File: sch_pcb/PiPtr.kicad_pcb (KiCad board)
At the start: 4 copper layers, 101.6 x 141.7 mm, 346 parts, among them J101 GLOBAL_LINK_LEFT, J102 GLOBAL_LINK_RIGHT, J107 RASPBERRY_PI, J111 FP_PIXEL, J112 AM2302, J113 I2C1_5V, J114 I2C0_3v3, J117 OLED_SSD1306, J204 DE9F, J301 SPARE, J302 SPARE, J303 SPARE, J304 SPARE, J305 AUX_IO_1, J306 SPARE, J307 SPARE, J308 AUX_IO_2, J309 SPARE, J310 SPARE, J313 SPARE, J314 SPARE, J404 DE9F, P301 Chassis, Q101 BSS138, Q102 BSS138, Q103 BSS138, Q104 BSS138, Q105 BSS138, Q201 2N7000, Q202 2N7000, Q203 2N7000, Q301 SPARE, Q302 SPARE, Q401 2N7000, Q402 2N7000, Q403 2N7000, U101 MCP23017, U102 IP4234CZ6, U103 MCP4351, U104 74HCT138, U105 74LV1T125, U107 MCP4351, U108 IP4234CZ6, U109 IP4234CZ6, U110 74LV1T125, U111 74LV1T125, U112 74LV1T125, U113 74LV1T125, U201 MCP6004N, U202 74LVC1G3157, U203 74LVC1G3157, U204 74LVC4066, U205 MCP6004N, U206 74LVC1G3157, U207 MCP6S26, U301 MCP23017, U302 SPARE, U303 SPARE, U304 MCP3008, U305 MCP1703A-2502/MB, U306 TPS54302, U307 IP4234CZ6, U401 MCP6004N, U402 74LVC1G3157, U403 74LVC1G3157, U404 74LVC4066, U405 MCP6004N, U406 74LVC1G3157, U407 MCP6S26, U501 CM108B, U502 CM108B, U503 TUSB2036, Y501 6MHz

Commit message: Add files via upload
Remove OLED connector
Remove extra bypass cap from third EEPOT
More routing - got the soundcards and usb hub done.  Only remaining big section is the DC-DC.  Still a bit of pain-in-the-tuchas traces that need to sneak across the board...
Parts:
- removed C110: 0.1u, lib:smd0603
- removed J114: I2C0_3v3, lib:SIL-6
- removed J117: OLED_SSD1306, lib:SIL-4
- removed TP105: TESTPOINT, lib:Wire_28AWG
- removed U109: IP4234CZ6, lib:SOT23-6
- added J103: RTC, lib:SIL-5, F.Cu at (104.1, 166.4)
- added R209: 10k, lib:smd0603, F.Cu at (78.0, 72.1)
- added R409: 10k, lib:smd0603, F.Cu at (142.8, 71.5)
- added R517: 15k, lib:smd0603, F.Cu at (95.0, 125.1)
- Q201, Q202, Q203, Q401, Q402, Q403: value 2N7000 -> BSS138
- moved C109 164.2 mm to (143.7, 63.1), turned to 270 degrees
- moved C307 151.0 mm to (108.7, 66.9), turned to 270 degrees
- moved C108 150.7 mm to (78.7, 63.6), turned to 270 degrees
- moved C306 148.8 mm to (105.9, 66.9), turned to 270 degrees
- moved C310 138.2 mm to (146.8, 107.9)
- moved C311 138.2 mm to (148.5, 107.9)
- moved C312 138.2 mm to (145.4, 107.8)
- moved C313 138.2 mm to (143.6, 107.8)
- moved R324 138.2 mm to (142.0, 107.8)
- moved U305 138.2 mm to (145.4, 103.3)
- moved J303 123.0 mm to (63.1, 129.9), turned to 90 degrees
- moved R306 120.4 mm to (60.1, 127.9), turned to 270 degrees
- moved R303 119.4 mm to (60.1, 130.9), turned to 270 degrees
- moved J302 118.0 mm to (63.1, 121.9), turned to 90 degrees
- moved C324 117.9 mm to (165.9, 136.6)
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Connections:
- U503 pad 6: +3V3 -> Net-(R517-Pad1)
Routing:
- net +3V3: track 15.1 -> 603.1 mm, vias 0 -> 8
- net /LINK2C: track 0.00 -> 127.0 mm, vias 0 -> 1
- net +5V: track 213.8 -> 339.5 mm, vias 9 -> 33
- net /SDA1_5: track 18.2 -> 141.7 mm, vias 2 -> 5
- net /LINK1C: track 0.00 -> 120.1 mm, vias 0 -> 1
- net /SCL1_5: track 21.0 -> 136.8 mm, vias 0 -> 4
- net GND: track 122.6 -> 235.6 mm, vias 65 -> 110
- net /~R47CS: track 0.00 -> 100.4 mm, vias 0 -> 4
- net SCLK_5: track 61.1 -> 160.0 mm, vias 2 -> 7
- net /~PGA2_CS: track 0.00 -> 89.9 mm, vias 0 -> 2
- net /CH2/TONE_FROM_PI: track 28.2 -> 102.8 mm, vias 2 -> 4
- net /~R03CS: track 0.00 -> 71.3 mm, vias 0 -> 4
- net /RX2_BUS1_EN: track 0.00 -> 69.1 mm, vias 0 -> 3
- net /RX2_BUS2_EN: track 0.00 -> 66.0 mm, vias 0 -> 3
- net /DHT_33: track 0.00 -> 64.4 mm, vias 0 -> 2
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- added copper zone on In2.Cu, net +5V
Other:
- board text added: "Pixel"
- board text added: "RTC"
- board text added: "Temp/Hum"

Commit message: Add files via upload
Fix sheet ordering in schematic
Finish routing (except USB connector...)
Still to do: USB connector, cleanup PCB, fix refdes positions
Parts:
- added LOGO301: MOUNTING_HOLE, lib:BOBCAT_LOGO, F.Cu at (154.8, 161.3)
- moved J307 71.7 mm to (108.3, 158.3)
- moved J306 56.4 mm to (92.5, 158.3)
- moved C308 48.2 mm to (131.8, 115.4), turned to 180 degrees
- moved C309 48.1 mm to (131.8, 113.9), turned to 180 degrees
- moved C322 22.5 mm to (143.3, 141.2), turned to 90 degrees
- moved C324 20.9 mm to (145.6, 141.2), turned to 90 degrees
- moved C323 17.9 mm to (147.8, 141.2), turned to 90 degrees
- moved C319 16.7 mm to (137.2, 140.9), turned to 180 degrees
- moved C325 16.0 mm to (149.8, 141.2), turned to 90 degrees
- moved C320 15.4 mm to (136.9, 143.1), turned to 180 degrees
- moved R327 11.8 mm to (135.9, 151.2), turned to 270 degrees
- moved R328 10.8 mm to (137.4, 151.2), turned to 90 degrees
- moved U306 6.54 mm to (136.9, 147.2), turned to 180 degrees
- moved R325 5.55 mm to (134.2, 148.2), turned to 90 degrees
- moved U105 5.28 mm to (94.8, 161.7)
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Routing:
- net /Spares, GPIO, and ADC/ADC_LIGHT: track 21.8 -> 248.7 mm, vias 0 -> 2
- net +2V5: track 52.9 -> 195.1 mm, vias 35 -> 37
- net /CH1/FROM_SOUNDCARD: track 0.00 -> 110.4 mm, vias 0 -> 6
- net +5V: track 339.5 -> 443.0 mm, vias 33 -> 43
- net /CH2/TO_SOUNDCARD: track 0.00 -> 95.6 mm, vias 0 -> 6
- net /CH2/FROM_SOUNDCARD: track 0.00 -> 94.5 mm, vias 0 -> 4
- net /SDA0_33: track 62.1 -> 143.3 mm, vias 0 -> 1
- net +12V: track 229.3 -> 306.6 mm, vias 1 -> 2
- net /CH1/TO_SOUNDCARD: track 0.00 -> 76.0 mm, vias 0 -> 2
- net /SCL0_33: track 59.7 -> 133.8 mm, vias 0 -> 1
- net MOSI_5: track 118.1 -> 185.3 mm, vias 4 -> 9
- net GND: track 235.6 -> 297.7 mm, vias 110 -> 123
- net MISO_5: track 76.6 -> 133.9 mm, vias 4 -> 7
- net /RX2_LOCAL_EN: track 17.9 -> 67.1 mm, vias 1 -> 4
- net +3V3: track 603.1 -> 631.6 mm, vias 8 -> 10
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- added copper zone on F.Cu, net +12V
- added copper zone on F.Cu, net +5V
- added copper zone on F.Cu, net GND
- added copper zone on B.Cu, net Net-(C321-Pad2)
- added copper zone on F.Cu, net Net-(C321-Pad2)
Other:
- net class Default: clearance 0.2 -> 0
- rule trace_clearance: 0.2 -> 0
- board text added: "MMRA PiPTR"
- board text removed: "LDR on front panel"

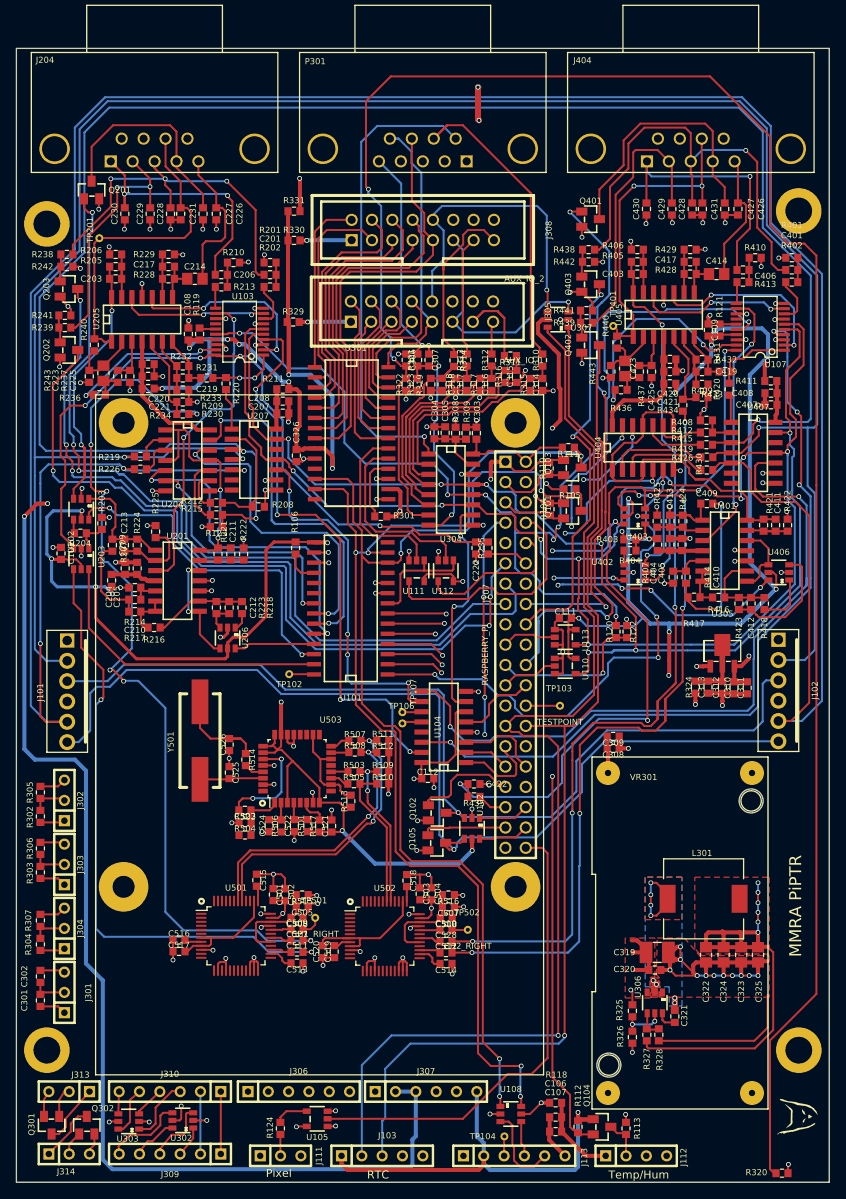
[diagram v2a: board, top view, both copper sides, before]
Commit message: Add files via upload
Add USB connector.  Pull back corner of board for it so the main board connector is around the same depth as the one on the Pi
Finish moving all refdes to avoid pads, other silk, and vias
Some routing cleanup
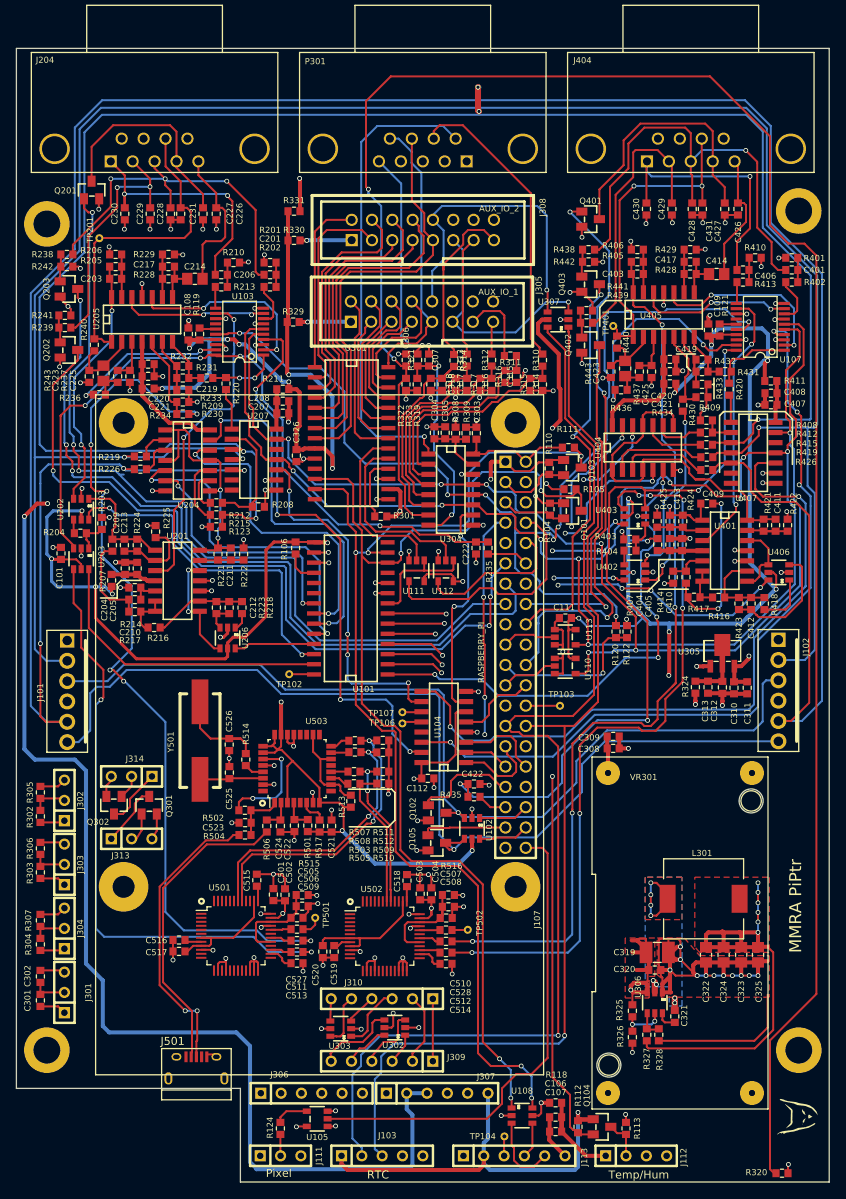
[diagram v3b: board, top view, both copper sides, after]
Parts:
- added J501: MicroUSB, lib:USB_Micro-B, F.Cu at (79.7, 155.3)
- moved J314 47.8 mm to (71.5, 118.9), turned to 180 degrees
- moved Q301 41.8 mm to (73.8, 122.5), turned to 180 degrees
- moved Q302 40.1 mm to (69.3, 122.5), turned to 0 degrees
- moved J313 32.5 mm to (71.5, 126.7), turned to 0 degrees
- moved J309 28.9 mm to (102.8, 154.5)
- moved J310 28.9 mm to (102.8, 146.7)
- moved U302 28.9 mm to (104.5, 150.3)
- moved U303 28.9 mm to (97.7, 150.5)
- moved R506 1.84 mm to (88.5, 125.1)
- moved J306 1.61 mm to (94.0, 158.5)
- moved J307 1.41 mm to (109.8, 158.5)
- moved U108 1.41 mm to (120.3, 161.3)
- moved C524 1.41 mm to (90.2, 125.1)
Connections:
- R504 pad 2: (no net) -> /soundcard/D_P
- R506 pad 2: (no net) -> /soundcard/D_N
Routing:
- net +12V: track 306.6 -> 268.2 mm
- net /soundcard/D_N: track 0.00 -> 38.2 mm
- net /soundcard/D_P: track 0.00 -> 36.4 mm, vias 0 -> 2
- net GND: track 297.7 -> 315.7 mm, vias 123 -> 122
- net /SDA1_5: track 152.5 -> 140.1 mm
- net +3V3: track 631.6 -> 620.6 mm
- net /RX1_BUS2_EN: track 55.2 -> 48.1 mm
- net /PTT2D: track 79.2 -> 73.1 mm
- net /Spares, GPIO, and ADC/ADC2: track 14.5 -> 9.85 mm
- net Net-(C203-Pad1): track 36.3 -> 32.2 mm
- net /CH1/FROM_SOUNDCARD: track 110.4 -> 114.2 mm
- net Net-(C315-Pad1): track 30.5 -> 26.9 mm
- net /RX2_LOCAL_EN: track 67.1 -> 63.6 mm
- net /CH2/TO_SOUNDCARD: track 95.6 -> 92.7 mm
- net /CH1/TONE_FROM_PI: track 92.2 -> 89.5 mm
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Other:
- outline, holes or cut-outs redrawn
- board text added: "MMRA PiPtr"
- board text removed: "MMRA PiPTR"

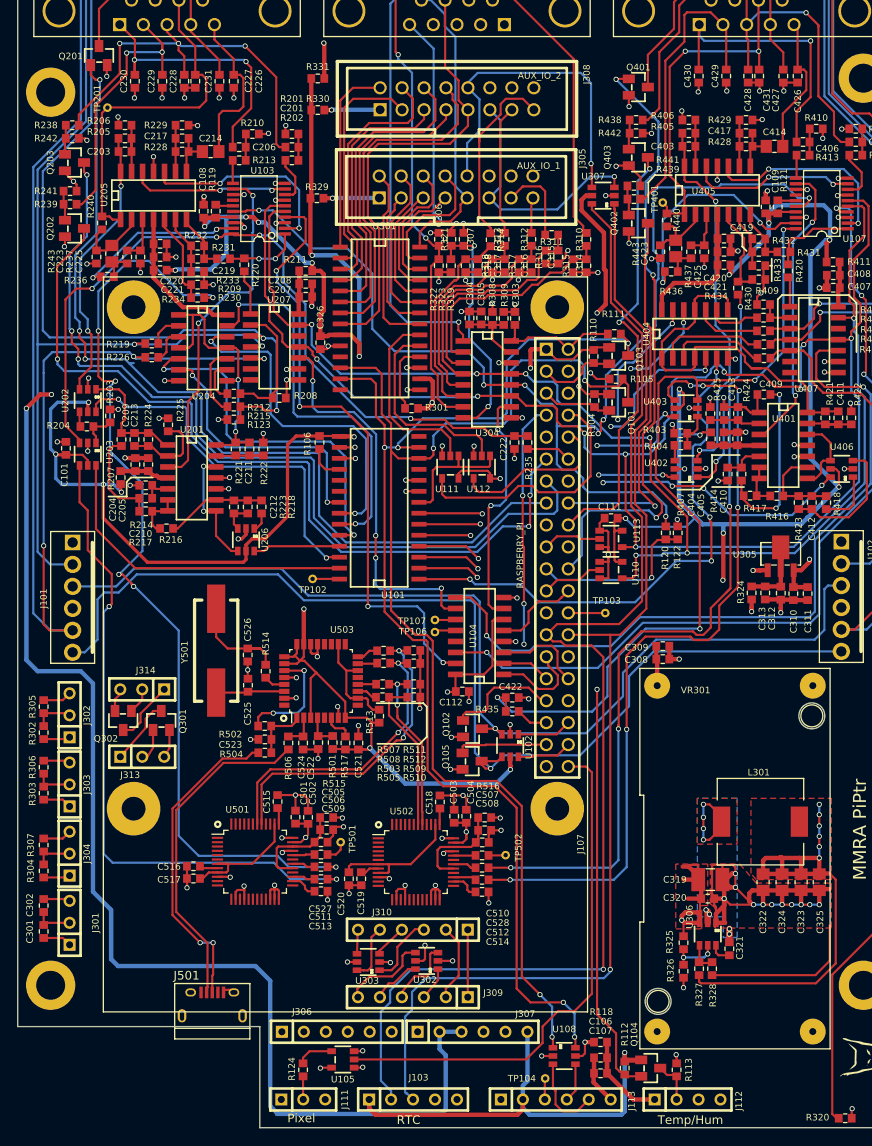
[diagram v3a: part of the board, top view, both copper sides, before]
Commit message: Flip pi
Whoops.  For all this time, the pi footprint was backwards, as if this board was a hat mounting on top of the pi.  Flip it so the pi mounts face down on this board.  This will put the network and usb connections towards the rear panel, so move it forward as far as possible to make room.
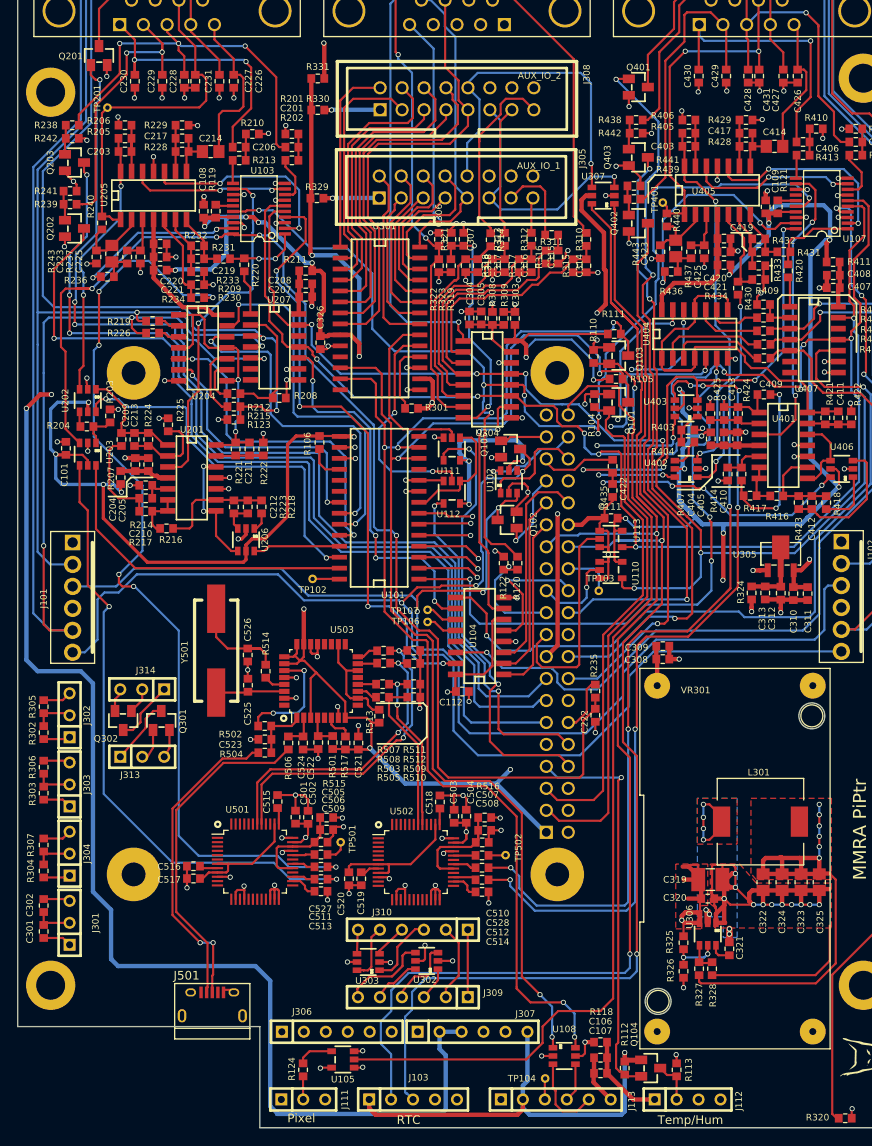
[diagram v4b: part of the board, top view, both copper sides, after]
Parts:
- J107: moved to B.Cu
- moved Q105 36.4 mm to (114.2, 91.1)
- moved C222 32.9 mm to (124.0, 121.9)
- moved R435 30.6 mm to (126.0, 93.1), turned to 270 degrees
- moved U102 30.5 mm to (114.0, 94.9), turned to 0 degrees
- moved R235 29.8 mm to (124.0, 119.1), turned to 270 degrees
- moved C422 26.6 mm to (126.0, 95.9), turned to 90 degrees
- moved Q102 24.5 mm to (113.8, 99.3), turned to 270 degrees
- moved R122 20.4 mm to (113.3, 104.3)
- moved R120 17.5 mm to (115.0, 104.3)
- moved J107 7.60 mm to (119.5, 111.3), turned to 90 degrees
- moved U112 4.53 mm to (107.3, 96.1)
- moved R226 2.80 mm to (72.8, 77.7)
- moved TP103 2.68 mm to (124.3, 107.5)
- moved R219 2.60 mm to (72.8, 76.3)
- moved U111 2.11 mm to (107.3, 91.1)
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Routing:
- net /SDA1_33: track 9.08 -> 66.7 mm, vias 0 -> 2
- net /CH1/TONE_FROM_PI: track 89.5 -> 145.7 mm
- net /PIXEL_33: track 60.4 -> 116.1 mm
- net /SCL1_33: track 8.10 -> 58.5 mm
- net +3V3: track 620.6 -> 670.3 mm, vias 10 -> 13
- net /DHT_33: track 87.7 -> 46.3 mm, vias 4 -> 1
- net /CH2/TONE_FROM_PI: track 98.1 -> 57.8 mm
- net /~CTCSS2: track 50.6 -> 73.0 mm, vias 2 -> 3
- net /LINK2C: track 126.8 -> 149.1 mm, vias 1 -> 3
- net /UINTA_33: track 29.6 -> 51.4 mm, vias 0 -> 2
- net /LINK1C: track 119.5 -> 141.2 mm, vias 1 -> 3
- net /UINTB_33: track 19.0 -> 39.3 mm, vias 0 -> 2
- net /COR2: track 44.6 -> 63.3 mm
- net /MOSI_33: track 6.80 -> 25.3 mm
- net /SELB_33: track 5.64 -> 21.4 mm
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
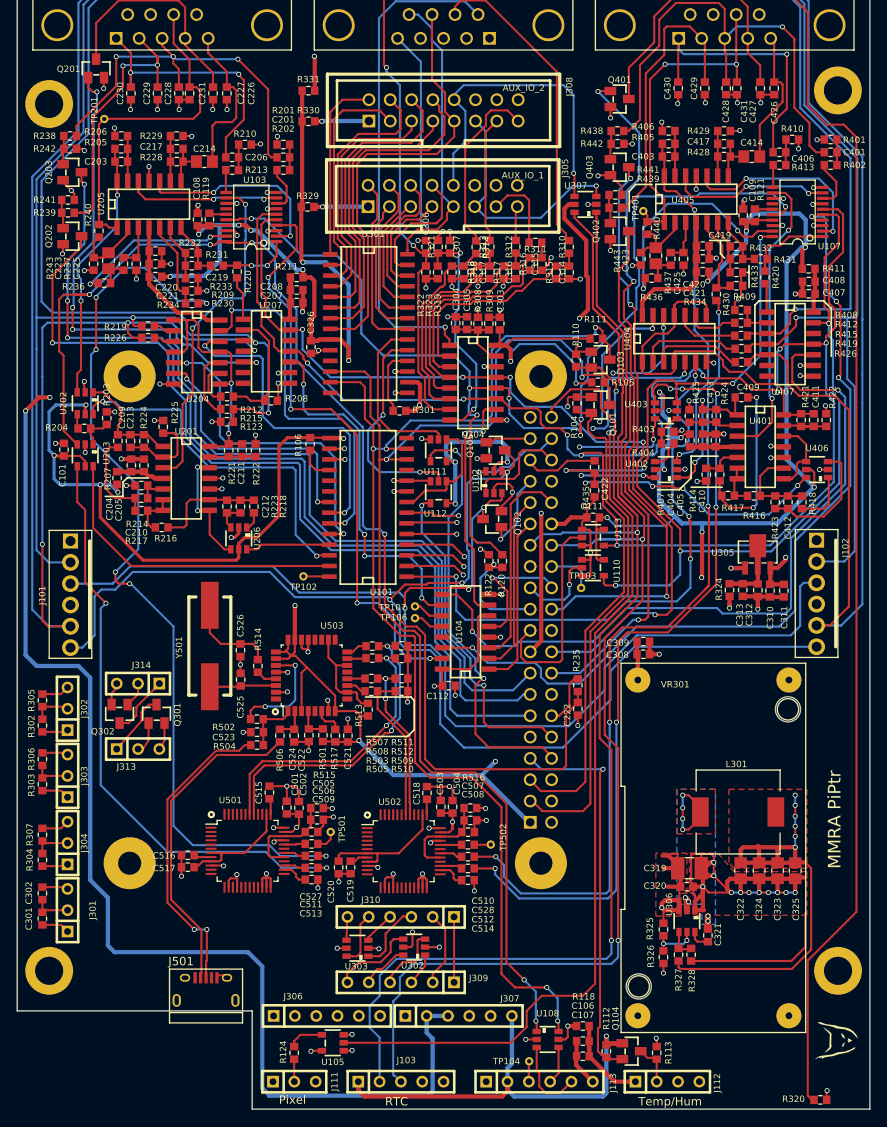
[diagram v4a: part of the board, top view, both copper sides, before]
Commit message: Silk cleanup
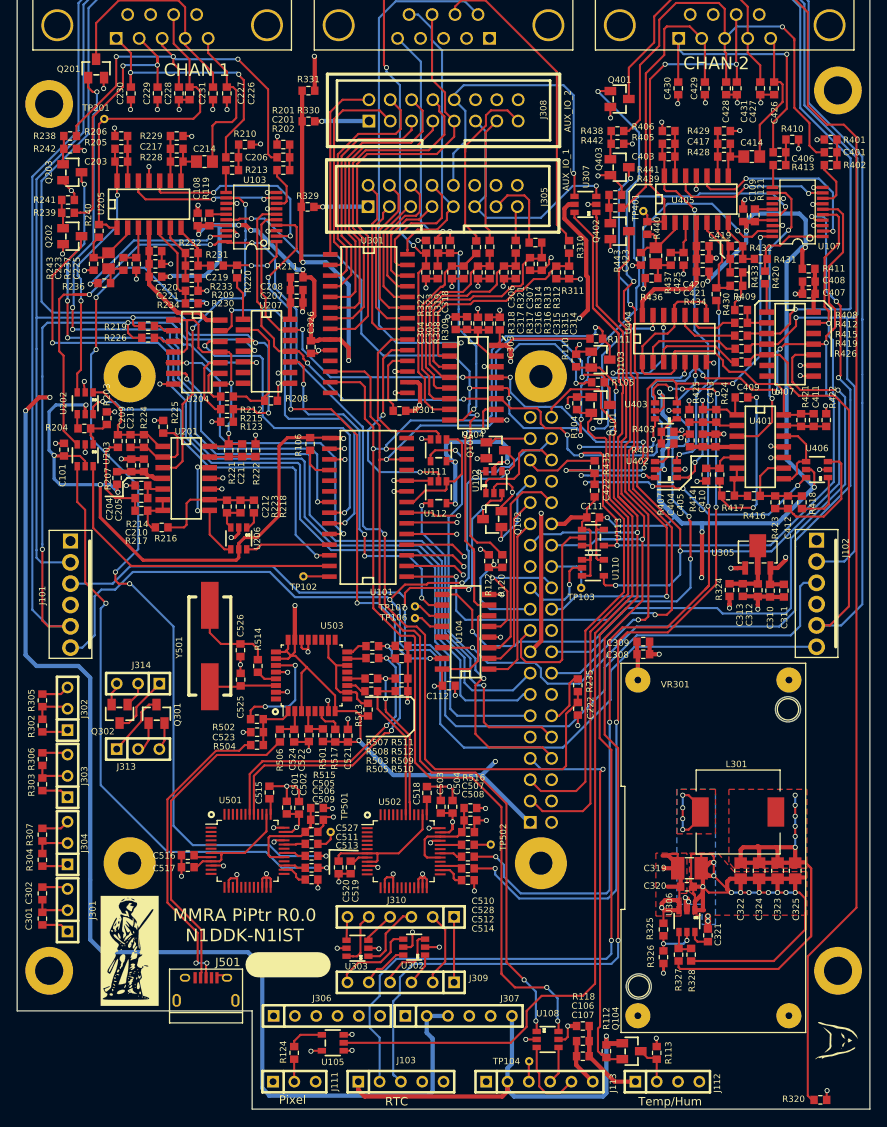
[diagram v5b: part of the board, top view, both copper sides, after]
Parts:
- added G***: LOGO, lib:mmra_logo1, F.Cu at (70.5, 150.7)
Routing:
- net GND: track 328.2 -> 343.1 mm
- net +5V: track 449.6 -> 457.8 mm
- net /Spares, GPIO, and ADC/ADC0: track 59.4 -> 62.2 mm
- net +3V3: track 670.3 -> 672.8 mm
- net +2V5: track 193.8 -> 194.6 mm
- net /LINK1_AUD: track 280.2 -> 280.7 mm
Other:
- board text added: "MMRA PiPtr R0.0 N1DDK-N1IST"
- board text removed: "MMRA PiPtr"
